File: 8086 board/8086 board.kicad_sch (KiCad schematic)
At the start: 59 parts, among them J1 USB_C_Receptacle_USB2.0, SW34 POWER, U1 P8086-2, U2 74AC00, U3 74HC14, U4 74HC02

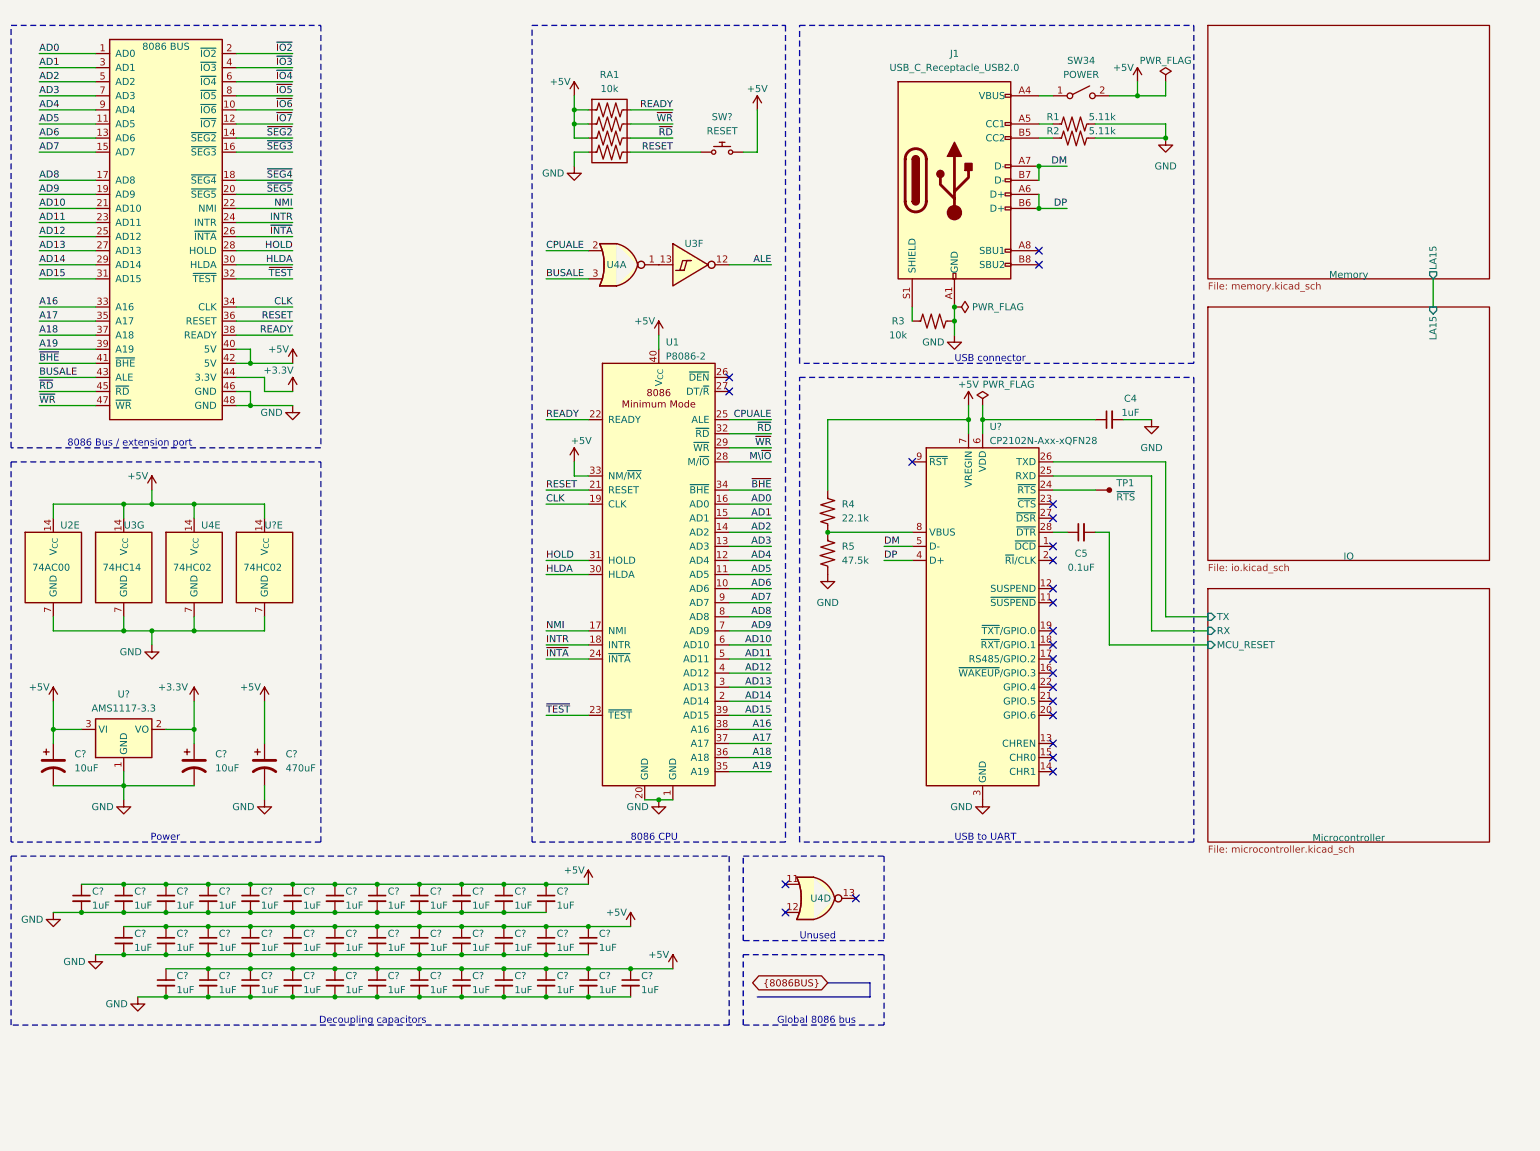
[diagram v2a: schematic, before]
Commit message: -remove power switch -add testpoints for unused logic gate
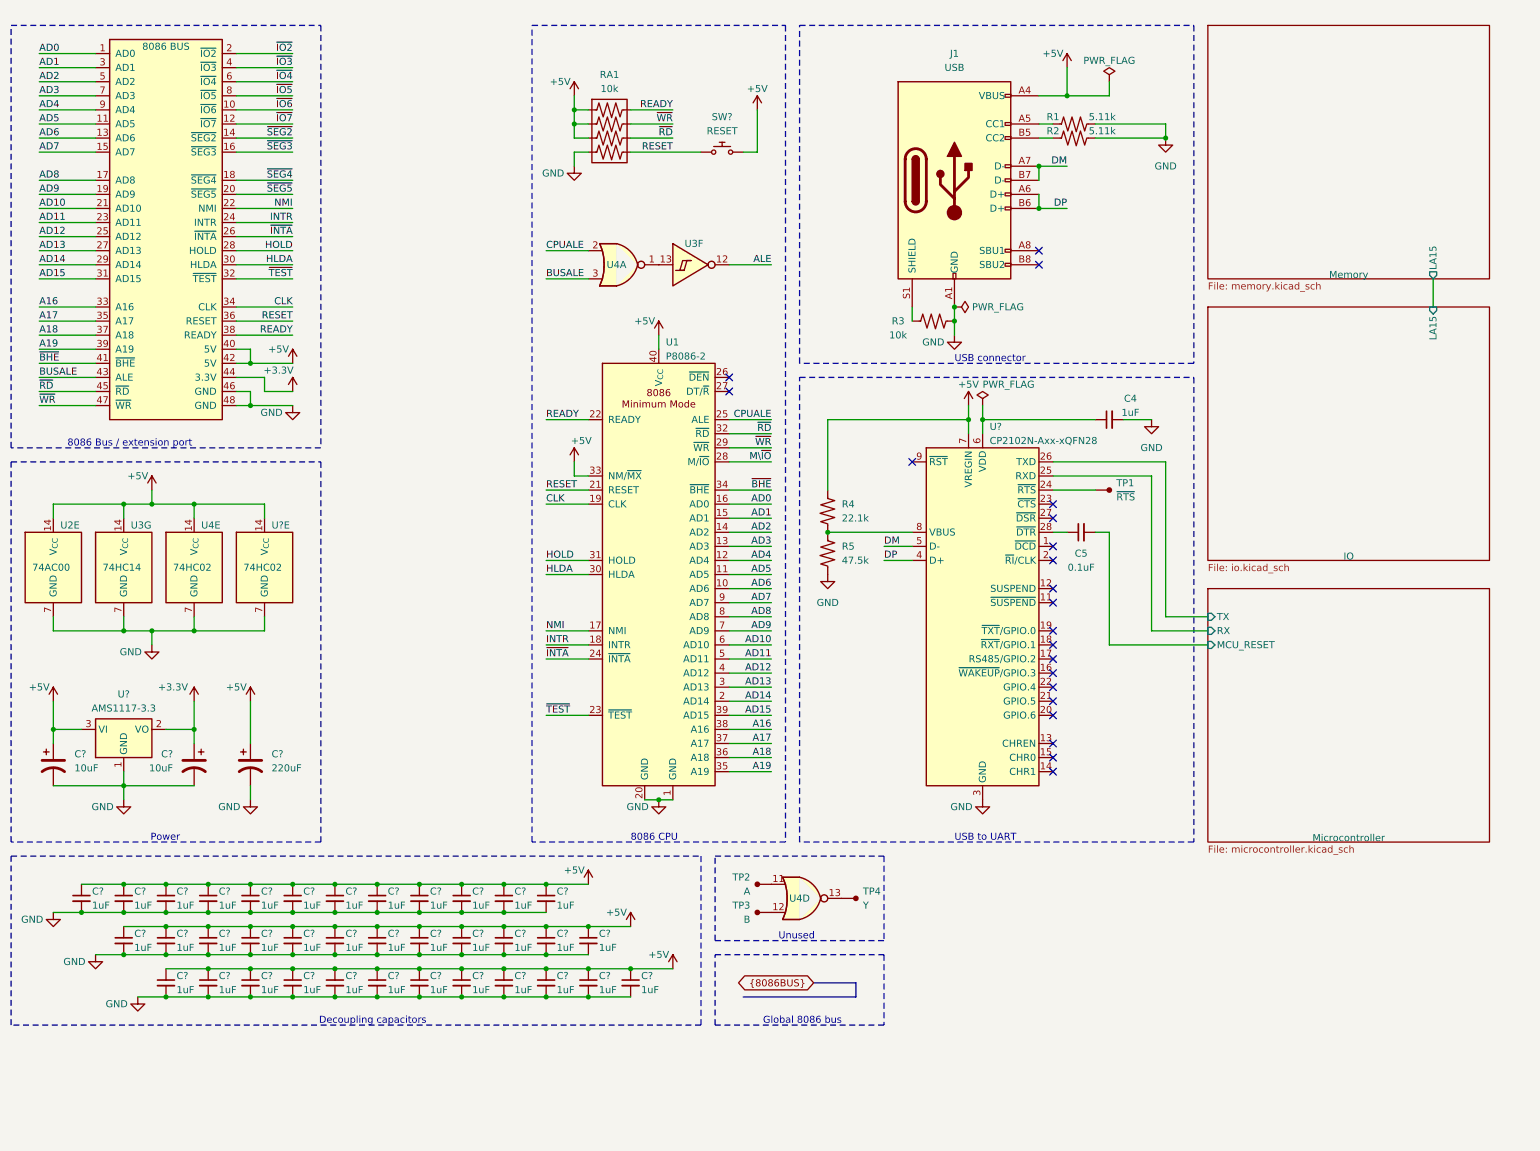
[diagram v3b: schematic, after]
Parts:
- removed SW34: POWER, symbol Switch:SW_SPST
- added TP2: A, TestPoint:TestPoint_Pad_1.5x1.5mm, symbol 8086PC:TestPoint
- added TP3: B, TestPoint:TestPoint_Pad_1.5x1.5mm, symbol 8086PC:TestPoint
- added TP4: Y, TestPoint:TestPoint_Pad_1.5x1.5mm, symbol 8086PC:TestPoint
- C?: value 470uF -> 220uF; footprint (none) -> Capacitor_Tantalum_SMD:CP_EIA-7343-43_Kemet-X_Pad2.25x2.55mm_HandSolder
- J1: value USB_C_Receptacle_USB2.0 -> USB
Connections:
- net +5V: now also J1.A4 (VBUS), J1.A9 (VBUS), J1.B4 (VBUS), J1.B9 (VBUS)
- net at U4.11: now also TP2.1
- net at U4.12: now also TP3.1
- net at U4.13: now also TP4.1
- no-connect marks 24 -> 21
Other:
- company: (none) -> Eldad Hellerman
- title: 8086 PCB -> 8086 computer
- moved on the sheet: C?, U4D

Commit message: change schematic to use new components
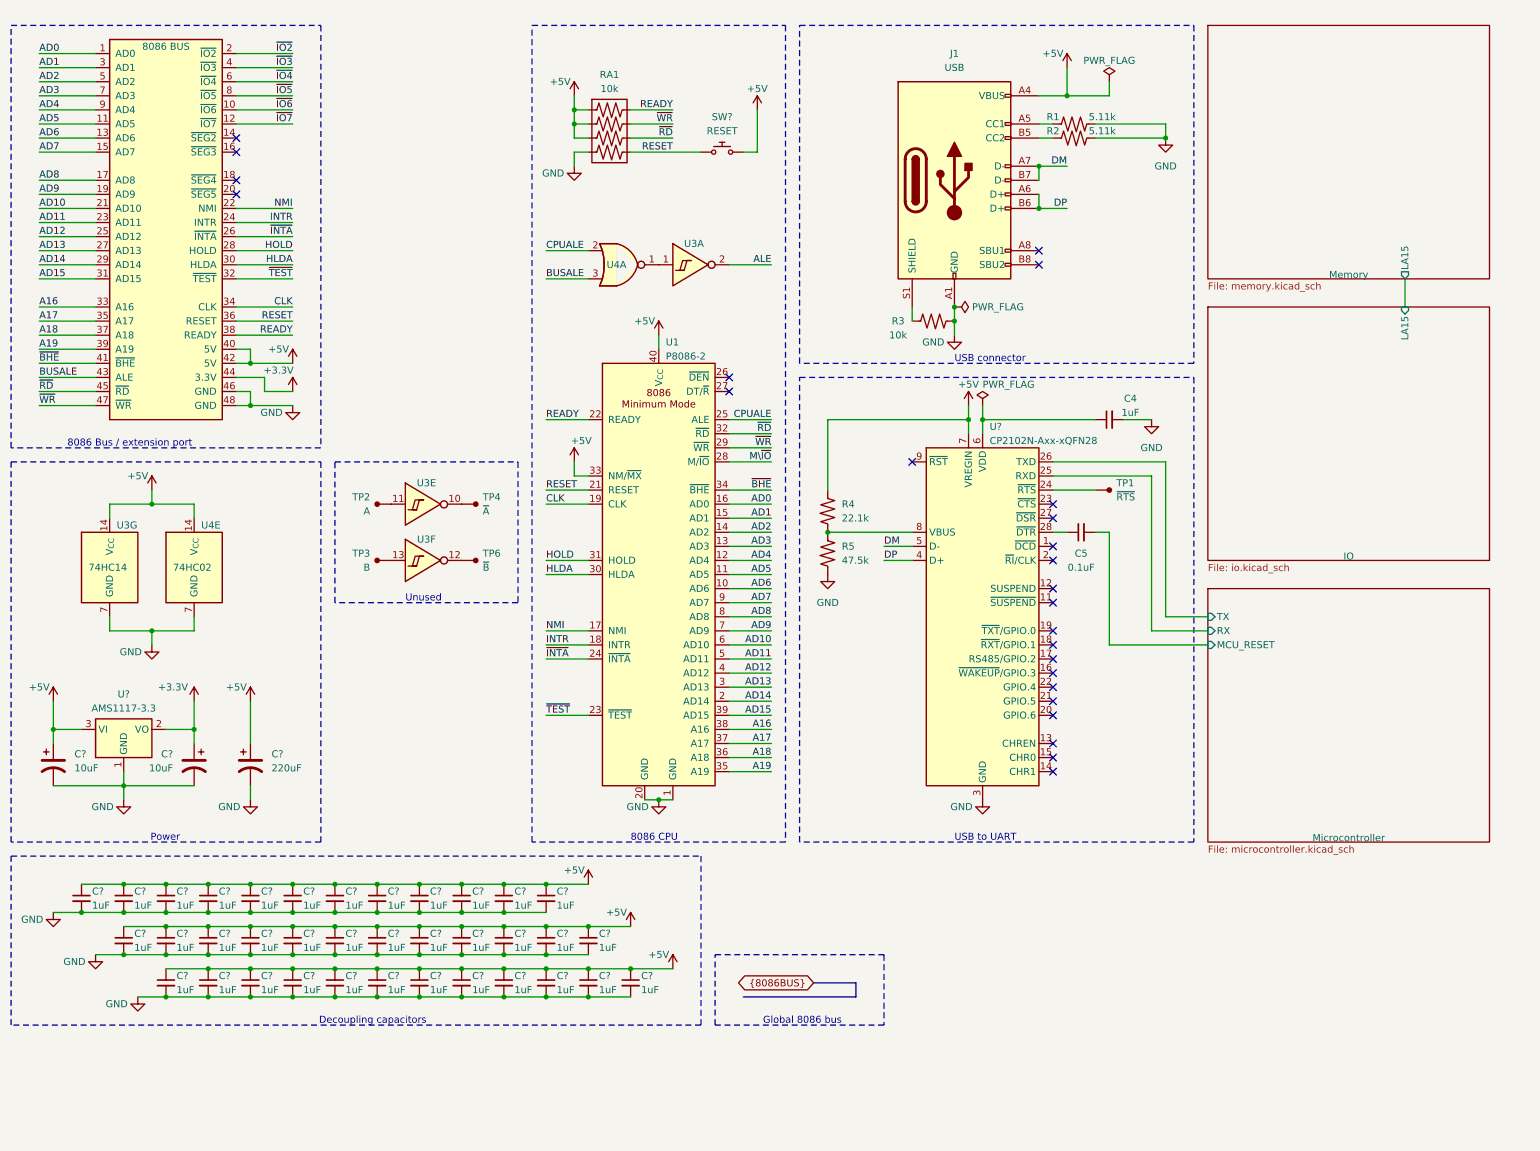
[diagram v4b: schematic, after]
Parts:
- removed U2: 74AC00, Package_SO:SOIC-14_3.9x8.7mm_P1.27mm, symbol 8086PC:74AC00
- removed unit 4 of U4
- removed U?: 74HC02, Package_SO:SOIC-14_3.9x8.7mm_P1.27mm, symbol 8086PC:74HC02
- added TP6: ~{B}, TestPoint:TestPoint_Pad_1.5x1.5mm, symbol 8086PC:TestPoint
- added unit 6 of U3
- added unit 5 of U3
- TP4: value Y -> ~{A}
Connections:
- net ALE: now also U3.2; no longer U3.12
- net at TP4.1: now also U3.10
- net at U4.1: now also U3.1; no longer U3.13
- net at TP2.1: now also U3.11
- net at TP3.1: now also U3.13
- net ~{SEG2}: no longer names the net of BUS1.14 (~{SEG2})
- net ~{SEG3}: no longer names the net of BUS1.16 (~{SEG3})
- net ~{SEG4}: no longer names the net of BUS1.18 (~{SEG4})
- net ~{SEG5}: no longer names the net of BUS1.20 (~{SEG5})
- new net: TP6.1, U3.12
- no-connect marks 21 -> 25
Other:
- moved on the sheet: TP2, TP3, U3G

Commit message: reduced schematic, PCB memory routed
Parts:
- removed TP2: A, TestPoint:TestPoint_Pad_1.5x1.5mm, symbol 8086PC:TestPoint
- removed TP3: B, TestPoint:TestPoint_Pad_1.5x1.5mm, symbol 8086PC:TestPoint
- removed TP4: ~{A}, TestPoint:TestPoint_Pad_1.5x1.5mm, symbol 8086PC:TestPoint
- removed TP6: ~{B}, TestPoint:TestPoint_Pad_1.5x1.5mm, symbol 8086PC:TestPoint
- removed U3: 74HC14, Package_SO:SOIC-14_3.9x8.7mm_P1.27mm, symbol 8086PC:74HC14
- removed U4: 74HC02, Package_SO:SOIC-14_3.9x8.7mm_P1.27mm, symbol 8086PC:74HC02
- added U2: 74HC32, Package_SO:TSSOP-14_4.4x5mm_P0.65mm, symbol 8086PC:74HC32
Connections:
- net +5V: now also U2.14 (V_{CC})
- net ALE: now also U2.3
- net BUSALE: now also U2.2
- net CPUALE: now also U2.1
- net GND: now also U2.7 (GND)
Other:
- sheet IO ports: added D/~{C}; removed LA15
- sheet Memory ports: added LA16; removed LA15
- note removed: "Unused"

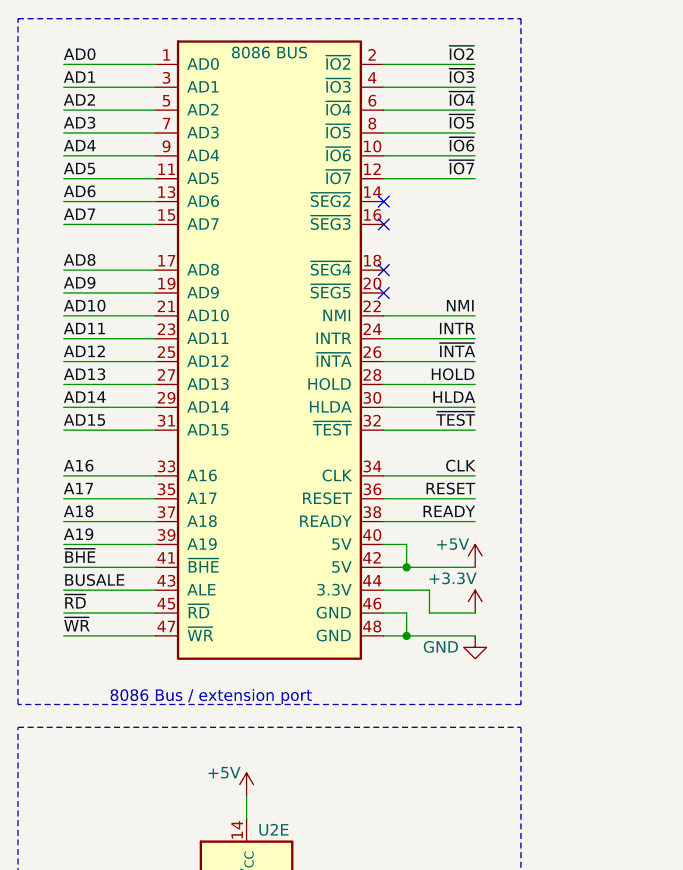
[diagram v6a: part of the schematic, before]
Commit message: schematic: reduced 8086 bus, no LCD shield
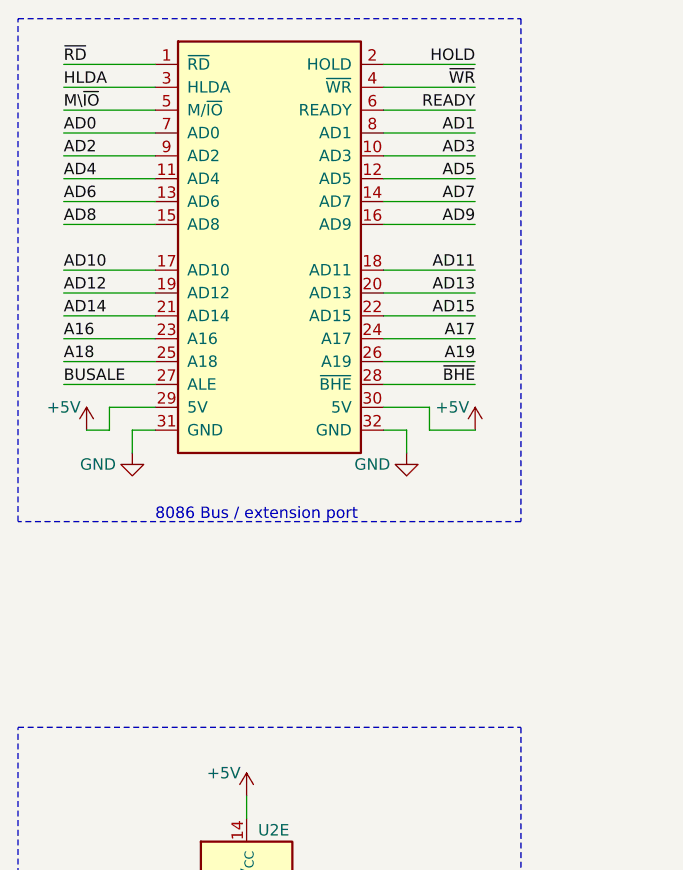
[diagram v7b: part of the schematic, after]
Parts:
- removed BUS1: 8086 BUS, Connector_PinHeader_2.54mm:PinHeader_2x24_P2.54mm_Vertical, symbol 8086PC:8086PC_BUS
- added BUS2: ~, Connector_PinHeader_2.54mm:PinHeader_2x16_P2.54mm_Vertical, symbol 8086PC:8086PC_BUS_REDUCED
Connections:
- net +5V: now also BUS2.29 (5V), BUS2.30 (5V)
- net A16: now also BUS2.23 (A16)
- net A17: now also BUS2.24 (A17)
- net A18: now also BUS2.25 (A18)
- net A19: now also BUS2.26 (A19)
- net AD0: now also BUS2.7 (AD0)
- net AD1: now also BUS2.8 (AD1)
- net AD10: now also BUS2.17 (AD10)
- net AD11: now also BUS2.18 (AD11)
- net AD12: now also BUS2.19 (AD12)
- net AD13: now also BUS2.20 (AD13)
- net AD14: now also BUS2.21 (AD14)
- net AD15: now also BUS2.22 (AD15)
- net AD2: now also BUS2.9 (AD2)
- net AD3: now also BUS2.10 (AD3)
- net AD4: now also BUS2.11 (AD4)
- net AD5: now also BUS2.12 (AD5)
- net AD6: now also BUS2.13 (AD6)
- net AD7: now also BUS2.14 (AD7)
- net AD8: now also BUS2.15 (AD8)
- net AD9: now also BUS2.16 (AD9)
- net BUSALE: now also BUS2.27 (ALE)
- net GND: now also BUS2.31 (GND), BUS2.32 (GND)
- net HLDA: now also BUS2.3 (HLDA)
- net HOLD: now also BUS2.2 (HOLD)
- net M\~{IO}: now also BUS2.5 (M/~{IO})
- net READY: now also BUS2.6 (READY)
- net ~{BHE}: now also BUS2.28 (~{BHE})
- net ~{RD}: now also BUS2.1 (~{RD})
- net ~{WR}: now also BUS2.4 (~{WR})
- no-connect marks 25 -> 21
